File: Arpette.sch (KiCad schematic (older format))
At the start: 18 parts, among them J3 40HAT, J6 CONN_02X02, J9 CONN_01X02, Q1 DMG2305UX, Q2 DMMT5401, U2 CAT24C32

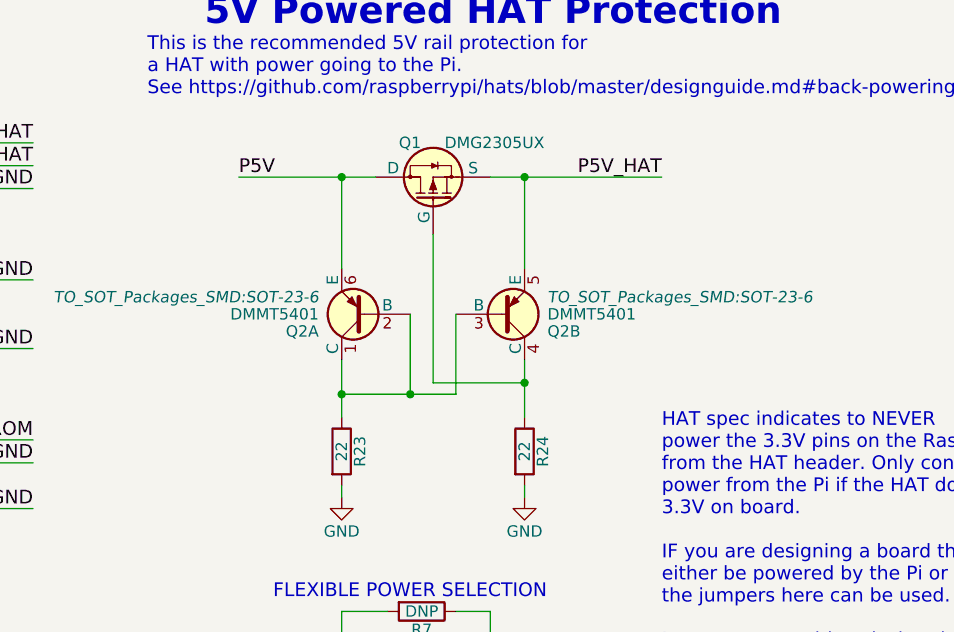
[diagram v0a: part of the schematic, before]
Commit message: Added multiple inputs
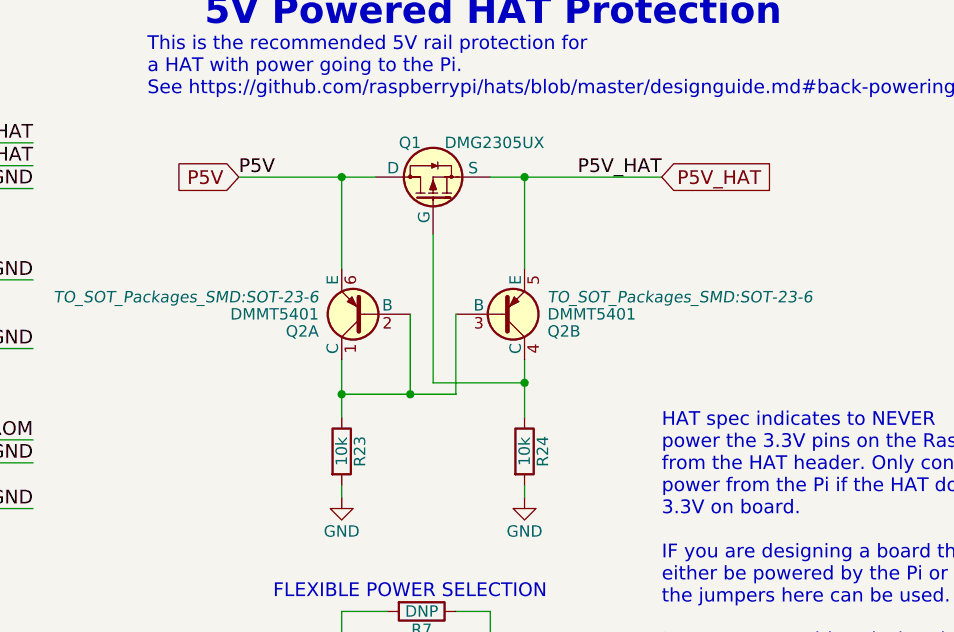
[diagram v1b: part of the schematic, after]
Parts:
- R23, R24: value 22 -> 10k
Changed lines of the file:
@@
 P 5750 3600
 F 0 "R23" V 5830 3600 50  0000 C CNN
-F 1 "22" V 5750 3600 50  0000 C CNN
+F 1 "10k" V 5750 3600 50  0000 C CNN
 F 2 "Resistors_SMD:R_0603_HandSoldering" V 5680 3600 50  0001 C CNN
 F 3 "" H 5750 3600 50  0001 C CNN
@@
 P 6550 3600
 F 0 "R24" V 6630 3600 50  0000 C CNN
-F 1 "22" V 6550 3600 50  0000 C CNN
+F 1 "10k" V 6550 3600 50  0000 C CNN
 F 2 "Resistors_SMD:R_0603_HandSoldering" V 6480 3600 50  0001 C CNN
 F 3 "" H 6550 3600 50  0001 C CNN
@@
 Wire Wire Line
 	3850 3050 3200 3050
+Text GLabel 5300 2400 0    60   Input ~ 0
+P5V
+Text GLabel 7150 2400 2    60   Input ~ 0
+P5V_HAT
 $EndSCHEMATC

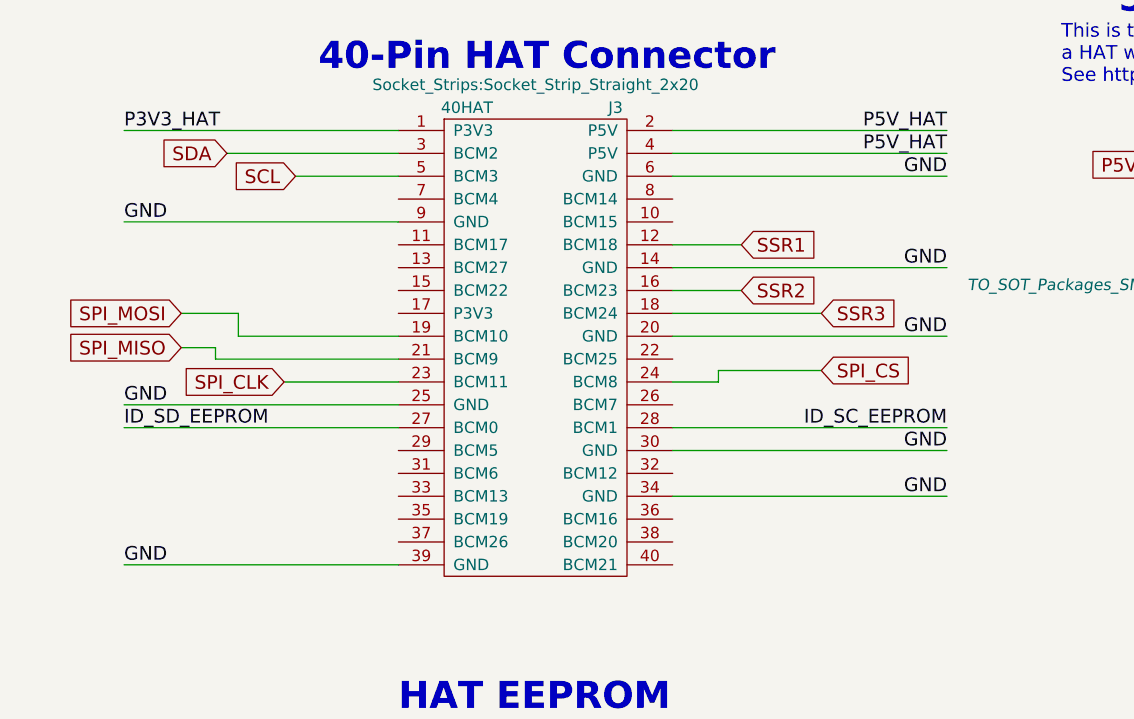
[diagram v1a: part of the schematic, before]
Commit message: Peripherals added
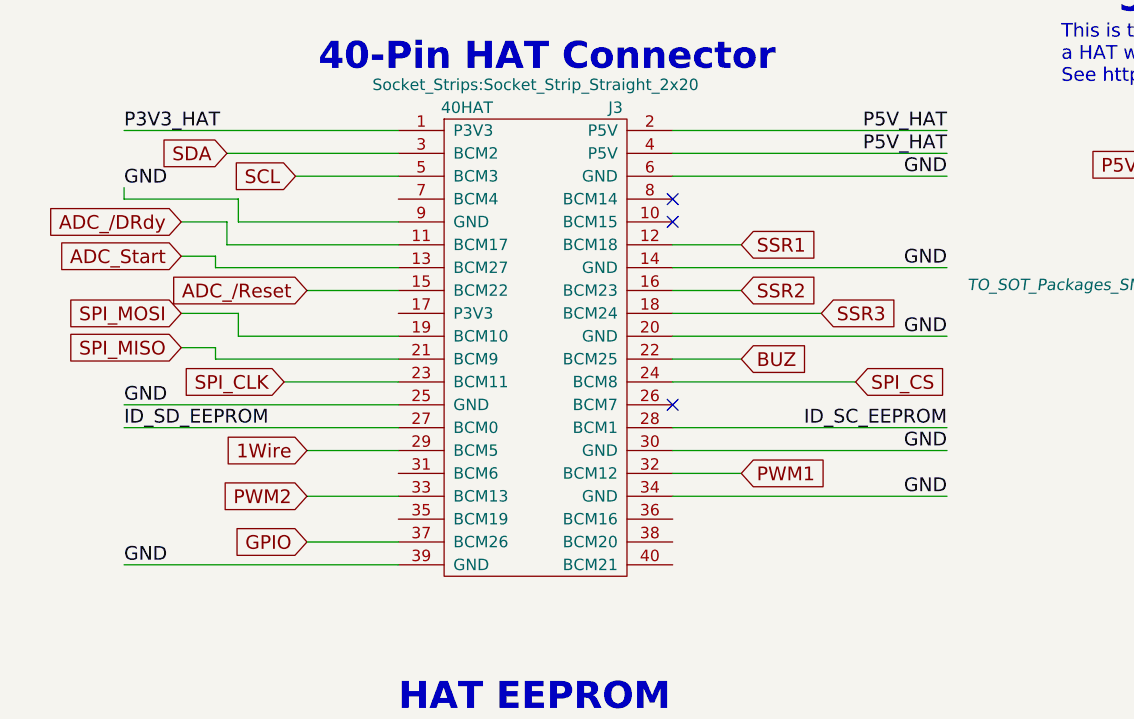
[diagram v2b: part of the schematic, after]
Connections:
- net ADC_/DRdy: now reaches J3.11 (BCM17)
- net ADC_Start: now reaches J3.13 (BCM27)
- net ADC_/Reset: now reaches J3.15 (BCM22)
- net BUZ: now reaches J3.22 (BCM25)
- net 1Wire: now reaches J3.29 (BCM5)
- net PWM1: now reaches J3.32 (BCM12)
- net PWM2: now reaches J3.33 (BCM13)
- net GPIO: now reaches J3.37 (BCM26)
- no-connect marks 0 -> 3
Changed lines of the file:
@@
 Wire Wire Line
 	2000 3450 800  3450
-Text Label 800  2650 0    60   ~ 0
+Text Label 800  2500 0    60   ~ 0
 GND
-Wire Wire Line
-	2000 2650 800  2650
 Text Label 800  2250 0    60   ~ 0
 P3V3_HAT
@@
 Wire Wire Line
 	1250 2350 2000 2350
-Text GLabel 3850 3300 2    60   Input ~ 0
+Text GLabel 4000 3350 2    60   Input ~ 0
 SPI_CS
 Wire Wire Line
-	3850 3300 3400 3300
-Wire Wire Line
-	3400 3300 3400 3350
-Wire Wire Line
-	3400 3350 3200 3350
+	3200 3350 4000 3350
 $Sheet
 S 10850 5500 3850 2200
@@
 Text GLabel 7150 2400 2    60   Input ~ 0
 P5V_HAT
+Text GLabel 1050 2650 0    60   Input ~ 0
+ADC_/DRdy
+Wire Wire Line
+	2000 2650 1300 2650
+Wire Wire Line
+	1300 2650 1300 2550
+Wire Wire Line
+	1300 2550 800  2550
+Wire Wire Line
+	800  2550 800  2500
+Wire Wire Line
+	1050 2650 1250 2650
+Wire Wire Line
+	1250 2650 1250 2750
+Wire Wire Line
+	1250 2750 2000 2750
+Text GLabel 1050 2800 0    60   Input ~ 0
+ADC_Start
+Text GLabel 1600 2950 0    60   Input ~ 0
+ADC_/Reset
+Wire Wire Line
+	2000 2950 1600 2950
+Wire Wire Line
+	2000 2850 1200 2850
+Wire Wire Line
+	1200 2850 1200 2800
+Wire Wire Line
+	1200 2800 1050 2800
+Text GLabel 3500 3250 2    60   Input ~ 0
+BUZ
+Wire Wire Line
+	3500 3250 3200 3250
+Text GLabel 3500 3750 2    60   Input ~ 0
+PWM1
+Wire Wire Line
+	3200 3750 3500 3750
+Text GLabel 1600 3650 0    60   Input ~ 0
+1Wire
+Wire Wire Line
+	1600 3650 2000 3650
+Text GLabel 1600 3850 0    60   Input ~ 0
+PWM2
+NoConn ~ 3200 3450
+NoConn ~ 3200 2650
+NoConn ~ 3200 2550
+Text GLabel 1600 4050 0    60   Input ~ 0
+GPIO
+Wire Wire Line
+	1600 4050 2000 4050
+Wire Wire Line
+	1600 3850 2000 3850
 $EndSCHEMATC

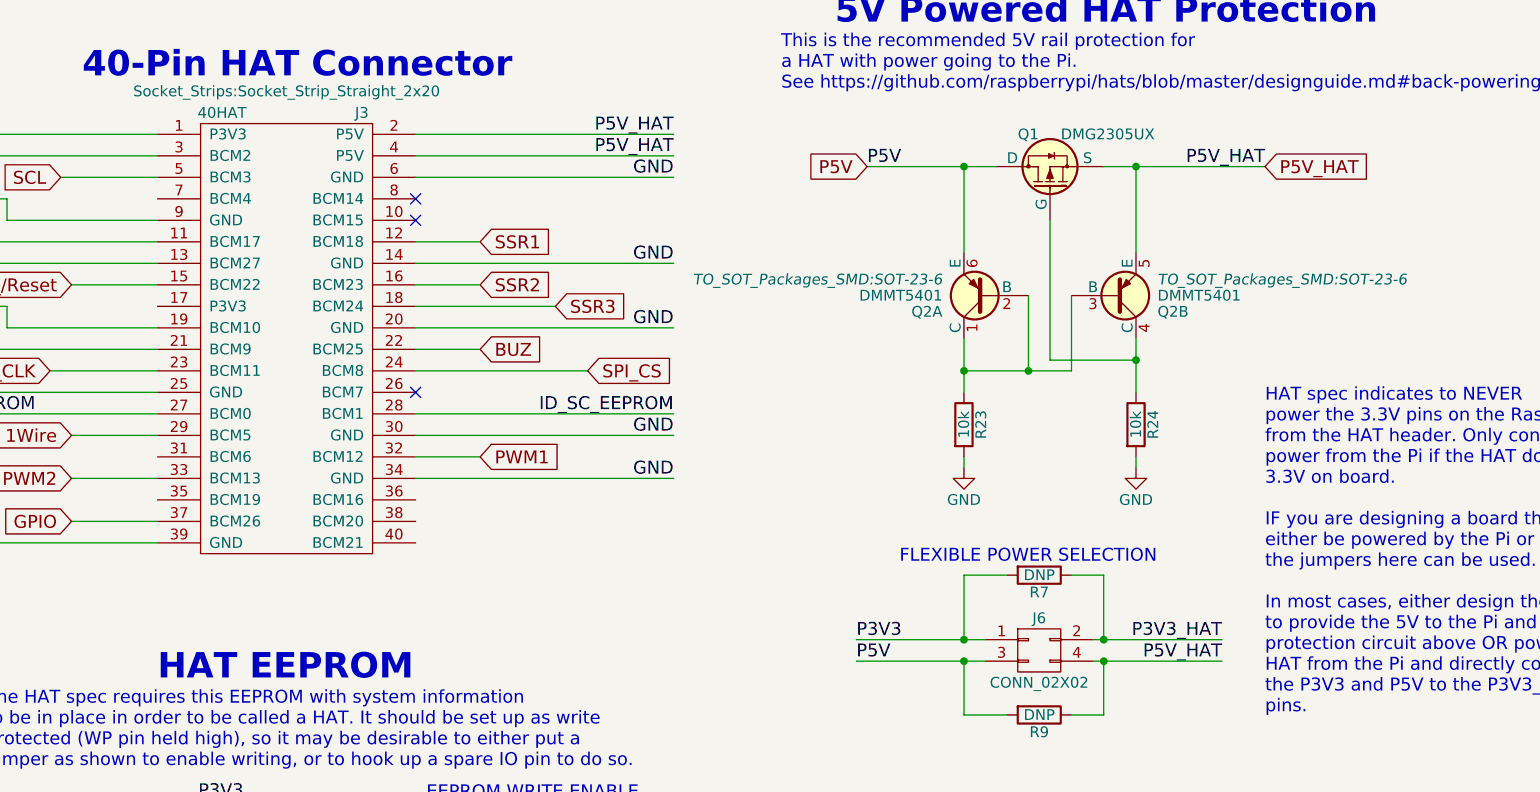
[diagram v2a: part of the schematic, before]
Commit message: ADC values
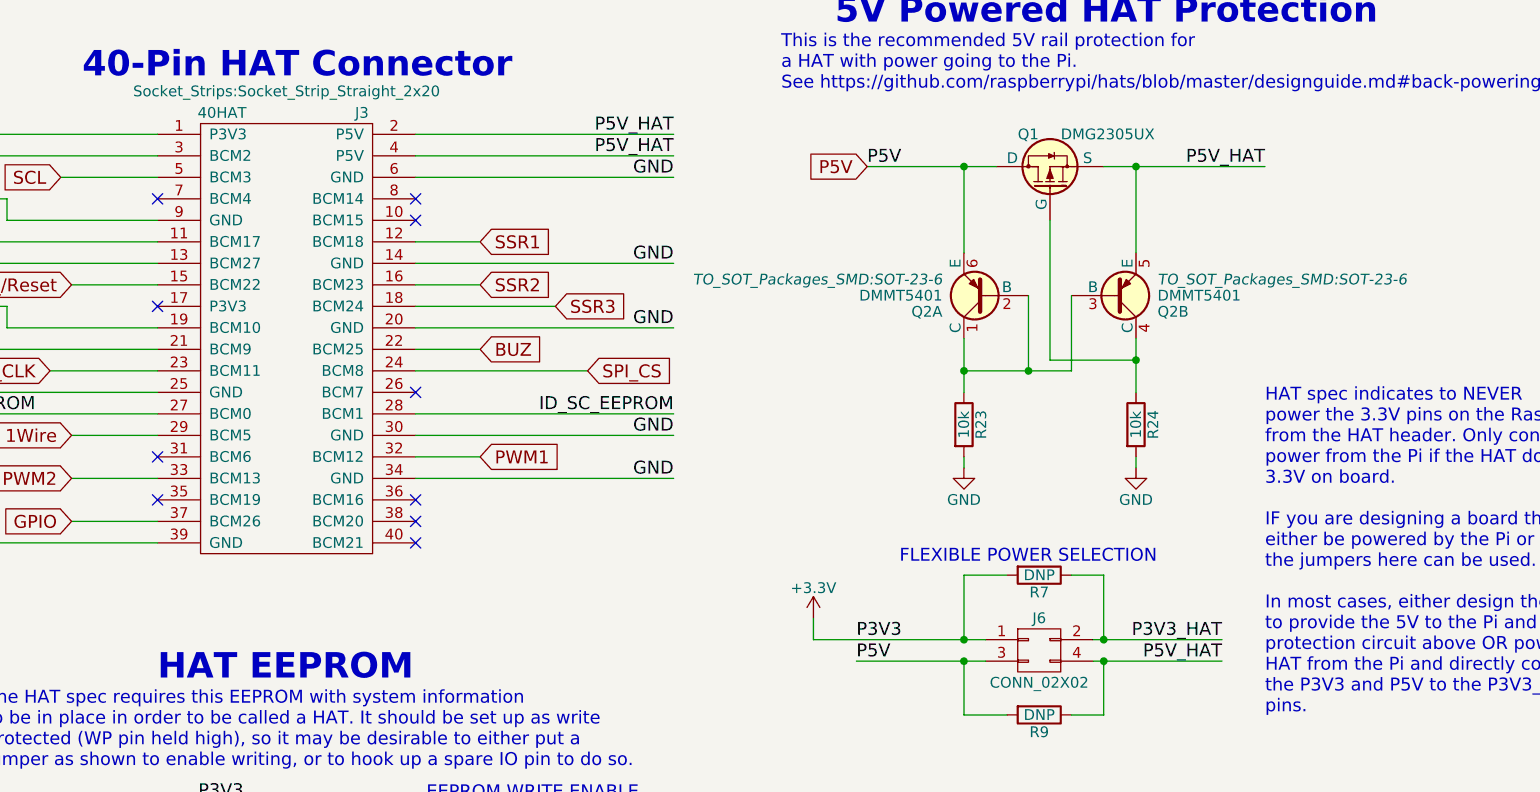
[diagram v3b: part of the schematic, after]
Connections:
- net P3V3 renamed +3V3
- no-connect marks 3 -> 10
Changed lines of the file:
@@
 P5V
 Wire Wire Line
-	5250 4600 5850 4600
+	5050 4600 5850 4600
 Wire Wire Line
 	5250 4700 5850 4700
@@
 Text GLabel 5300 2400 0    60   Input ~ 0
 P5V
-Text GLabel 7150 2400 2    60   Input ~ 0
-P5V_HAT
 Text GLabel 1050 2650 0    60   Input ~ 0
 ADC_/DRdy
@@
 Wire Wire Line
 	1600 3850 2000 3850
+NoConn ~ 3200 4150
+NoConn ~ 3200 4050
+NoConn ~ 3200 3950
+NoConn ~ 2000 2550
+NoConn ~ 2000 3050
+NoConn ~ 2000 3750
+NoConn ~ 2000 3950
+$Comp
+L +3.3V #PWR06
+U 1 1 59BAA317
+P 5050 4500
+F 0 "#PWR06" H 5050 4350 50  0001 C CNN
+F 1 "+3.3V" H 5050 4640 50  0000 C CNN
+F 2 "" H 5050 4500 50  0001 C CNN
+F 3 "" H 5050 4500 50  0001 C CNN
+	1    5050 4500
+	1    0    0    -1
+$EndComp
+Wire Wire Line
+	5050 4600 5050 4500
 $EndSCHEMATC

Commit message: BOM
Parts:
- Q1: renamed from Q2; footprint TO_SOT_Packages_SMD:SOT-23-6 -> TO_SOT_Packages_SMD:SOT-23-6_Handsoldering
- Q2: renamed from Q1; footprint TO_SOT_Packages_SMD:SOT-23 -> TO_SOT_Packages_SMD:SOT-23_Handsoldering
- renumbered H3 to H2, H2 to H3, J9 to J1, J3 to J2, J6 to J3, R11 to R1, R29 to R2, R6 to R3, R8 to R4, R23 to R5, R7 to R6, R9 to R7, R24 to R8, U2 to U1
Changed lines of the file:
@@
 $EndComp
 $Comp
-L 3mm_Mounting_Hole H2
+L 3mm_Mounting_Hole H3
 U 1 1 5834BCDF
 P 6650 6000
-F 0 "H2" H 6500 6100 60  0000 C CNN
+F 0 "H3" H 6500 6100 60  0000 C CNN
 F 1 "3mm_Mounting_Hole" H 6650 5850 60  0000 C CNN
 F 2 "project_footprints:NPTH_3mm_ID" H 6550 6000 60  0001 C CNN
@@
 $EndComp
 $Comp
-L 3mm_Mounting_Hole H3
+L 3mm_Mounting_Hole H2
 U 1 1 5834BD62
 P 5650 6550
-F 0 "H3" H 5500 6650 60  0000 C CNN
+F 0 "H2" H 5500 6650 60  0000 C CNN
 F 1 "3mm_Mounting_Hole" H 5650 6400 60  0000 C CNN
 F 2 "project_footprints:NPTH_3mm_ID" H 5550 6550 60  0001 C CNN
@@
 $EndComp
 $Comp
-L OX40HAT J3
+L OX40HAT J2
 U 1 1 58DFC771
 P 2600 2250
-F 0 "J3" H 2950 2350 50  0000 C CNN
+F 0 "J2" H 2950 2350 50  0000 C CNN
 F 1 "40HAT" H 2300 2350 50  0000 C CNN
 F 2 "Socket_Strips:Socket_Strip_Straight_2x20" H 2600 2450 50  0000 C CNN
@@
 P3V3
 $Comp
-L CONN_02X02 J6
+L CONN_02X02 J3
 U 1 1 58E13683
 P 6100 4650
-F 0 "J6" H 6100 4800 50  0000 C CNN
+F 0 "J3" H 6100 4800 50  0000 C CNN
 F 1 "CONN_02X02" H 6100 4500 50  0000 C CNN
 F 2 "Pin_Headers:Pin_Header_Straight_2x02" H 6100 3450 50  0001 C CNN
@@
 This is the recommended 5V rail protection for \na HAT with power going to the Pi.\nSee https://github.com/raspberrypi/hats/blob/master/designguide.md#back-powering-the-pi-via-the-j8-gpio-header
 $Comp
-L DMG2305UX Q1
+L DMG2305UX Q2
 U 1 1 58E14EB1
 P 6150 2400
-F 0 "Q1" V 6300 2550 50  0000 R CNN
+F 0 "Q2" V 6300 2550 50  0000 R CNN
 F 1 "DMG2305UX" V 6300 2350 50  0000 R CNN
-F 2 "TO_SOT_Packages_SMD:SOT-23" H 6350 2500 50  0001 C CNN
+F 2 "TO_SOT_Packages_SMD:SOT-23_Handsoldering" H 6350 2500 50  0001 C CNN
 F 3 "" H 6150 2400 50  0000 C CNN
 	1    6150 2400
@@
 $EndComp
 $Comp
-L DMMT5401 Q2
+L DMMT5401 Q1
 U 1 1 58E1538B
 P 5850 3000
-F 0 "Q2" H 6050 3075 50  0000 L CNN
+F 0 "Q1" H 6050 3075 50  0000 L CNN
 F 1 "DMMT5401" H 6050 3000 50  0000 L CNN
-F 2 "TO_SOT_Packages_SMD:SOT-23-6" H 6050 2925 50  0000 L CIN
+F 2 "TO_SOT_Packages_SMD:SOT-23-6_Handsoldering" H 6050 2925 50  0000 L CIN
 F 3 "" H 5850 3000 50  0000 L CNN
 	1    5850 3000
@@
 $EndComp
 $Comp
-L DMMT5401 Q2
+L DMMT5401 Q1
 U 2 1 58E153D6
 P 6450 3000
-F 0 "Q2" H 6650 3075 50  0000 L CNN
+F 0 "Q1" H 6650 3075 50  0000 L CNN
 F 1 "DMMT5401" H 6650 3000 50  0000 L CNN
-F 2 "TO_SOT_Packages_SMD:SOT-23-6" H 6650 2925 50  0000 L CIN
+F 2 "TO_SOT_Packages_SMD:SOT-23-6_Handsoldering" H 6650 2925 50  0000 L CIN
 F 3 "" H 6450 3000 50  0000 L CNN
 	2    6450 3000
@@
 $EndComp
 $Comp
-L R R23
+L R R5
 U 1 1 58E15896
 P 5750 3600
-F 0 "R23" V 5830 3600 50  0000 C CNN
+F 0 "R5" V 5830 3600 50  0000 C CNN
 F 1 "10k" V 5750 3600 50  0000 C CNN
 F 2 "Resistors_SMD:R_0603_HandSoldering" V 5680 3600 50  0001 C CNN
@@
 $EndComp
 $Comp
-L R R24
+L R R8
 U 1 1 58E158A1
 P 6550 3600
-F 0 "R24" V 6630 3600 50  0000 C CNN
+F 0 "R8" V 6630 3600 50  0000 C CNN
 F 1 "10k" V 6550 3600 50  0000 C CNN
 F 2 "Resistors_SMD:R_0603_HandSoldering" V 6480 3600 50  0001 C CNN
@@
 Connection ~ 6550 2400
 $Comp
-L CAT24C32 U2
+L CAT24C32 U1
 U 1 1 58E1713F
 P 2100 5850
-F 0 "U2" H 2450 6200 50  0000 C CNN
+F 0 "U1" H 2450 6200 50  0000 C CNN
 F 1 "CAT24C32" H 1850 6200 50  0000 C CNN
 F 2 "Housings_SOIC:SOIC-8_3.9x4.9mm_Pitch1.27mm" H 2100 5850 50  0001 C CNN
@@
 $EndComp
 $Comp
-L R R6
+L R R3
 U 1 1 58E17715
 P 2350 7400
-F 0 "R6" V 2430 7400 50  0000 C CNN
+F 0 "R3" V 2430 7400 50  0000 C CNN
 F 1 "3.9K" V 2350 7400 50  0000 C CNN
 F 2 "Resistors_SMD:R_0603_HandSoldering" V 2280 7400 50  0001 C CNN
@@
 $EndComp
 $Comp
-L R R8
+L R R4
 U 1 1 58E17720
 P 2350 7650
-F 0 "R8" V 2430 7650 50  0000 C CNN
+F 0 "R4" V 2430 7650 50  0000 C CNN
 F 1 "3.9K" V 2350 7650 50  0000 C CNN
 F 2 "Resistors_SMD:R_0603_HandSoldering" V 2280 7650 50  0001 C CNN
@@
 ID_SC_EEPROM_pu
 $Comp
-L CONN_01X02 J9
+L CONN_01X02 J1
 U 1 1 58E18D32
 P 750 6050
-F 0 "J9" H 750 6200 50  0000 C CNN
+F 0 "J1" H 750 6200 50  0000 C CNN
 F 1 "CONN_01X02" V 850 6050 50  0000 C CNN
 F 2 "Pin_Headers:Pin_Header_Straight_1x02" H 750 6050 50  0001 C CNN
@@
 $EndComp
 $Comp
-L R R29
+L R R2
 U 1 1 58E19E51
 P 1550 6250
-F 0 "R29" V 1630 6250 50  0000 C CNN
+F 0 "R2" V 1630 6250 50  0000 C CNN
 F 1 "10K" V 1550 6250 50  0000 C CNN
 F 2 "Resistors_SMD:R_0603_HandSoldering" V 1480 6250 50  0001 C CNN
@@
 EEPROM WRITE ENABLE
 $Comp
-L R R7
+L R R6
 U 1 1 58E22085
 P 6100 4300
-F 0 "R7" V 6180 4300 50  0000 C CNN
+F 0 "R6" V 6180 4300 50  0000 C CNN
 F 1 "DNP" V 6100 4300 50  0000 C CNN
 F 2 "Resistors_SMD:R_0805_HandSoldering" V 6030 4300 50  0001 C CNN
@@
 $EndComp
 $Comp
-L R R9
+L R R7
 U 1 1 58E2218F
 P 6100 4950
-F 0 "R9" V 6180 4950 50  0000 C CNN
+F 0 "R7" V 6180 4950 50  0000 C CNN
 F 1 "DNP" V 6100 4950 50  0000 C CNN
 F 2 "Resistors_SMD:R_0805_HandSoldering" V 6030 4950 50  0001 C CNN
@@
 Connection ~ 5750 4600
 $Comp
-L R R11
+L R R1
 U 1 1 58E22900
 P 1300 6100
-F 0 "R11" V 1380 6100 50  0000 C CNN
+F 0 "R1" V 1380 6100 50  0000 C CNN
 F 1 "DNP" V 1300 6100 50  0000 C CNN
 F 2 "Resistors_SMD:R_0805_HandSoldering" V 1230 6100 50  0001 C CNN

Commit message: PCB created
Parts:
- J1: footprint Pin_Headers:Pin_Header_Straight_1x02 -> Pin_Headers:Pin_Header_Straight_1x02_Pitch1.27mm
- J2: footprint Socket_Strips:Socket_Strip_Straight_2x20 -> Pin_Headers:Pin_Header_Straight_2x20_Pitch2.54mm
- J3: footprint Pin_Headers:Pin_Header_Straight_2x02 -> Pin_Headers:Pin_Header_Straight_2x02_Pitch1.27mm
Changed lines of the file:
@@
 F 0 "J2" H 2950 2350 50  0000 C CNN
 F 1 "40HAT" H 2300 2350 50  0000 C CNN
-F 2 "Socket_Strips:Socket_Strip_Straight_2x20" H 2600 2450 50  0000 C CNN
+F 2 "Pin_Headers:Pin_Header_Straight_2x20_Pitch2.54mm" H 2600 2450 50  0000 C CNN
 F 3 "" H 1900 2250 50  0000 C CNN
 	1    2600 2250
@@
 F 0 "J3" H 6100 4800 50  0000 C CNN
 F 1 "CONN_02X02" H 6100 4500 50  0000 C CNN
-F 2 "Pin_Headers:Pin_Header_Straight_2x02" H 6100 3450 50  0001 C CNN
+F 2 "Pin_Headers:Pin_Header_Straight_2x02_Pitch1.27mm" H 6100 3450 50  0001 C CNN
 F 3 "" H 6100 3450 50  0000 C CNN
 	1    6100 4650
@@
 F 0 "J1" H 750 6200 50  0000 C CNN
 F 1 "CONN_01X02" V 850 6050 50  0000 C CNN
-F 2 "Pin_Headers:Pin_Header_Straight_1x02" H 750 6050 50  0001 C CNN
+F 2 "Pin_Headers:Pin_Header_Straight_1x02_Pitch1.27mm" H 750 6050 50  0001 C CNN
 F 3 "" H 750 6050 50  0000 C CNN
 	1    750  6050
